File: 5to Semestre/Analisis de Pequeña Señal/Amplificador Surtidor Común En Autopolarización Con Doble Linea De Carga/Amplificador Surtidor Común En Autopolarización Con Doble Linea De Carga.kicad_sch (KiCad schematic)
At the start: 9 parts, among them Q1 NJFET

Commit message: añadiendo Rc para simulaciones con carga y uso de etiquetas
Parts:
- added Rc1: 100k, symbol Device:R
- Rd1: renamed from R2; value 6k -> 1k
- Rs1: renamed from R3; value 300 -> 1k
- renumbered R1 to Rg1
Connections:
- net 0: now also Rc1.2
- net Vdd: now reaches Rd1.1, V2.1
- net Vo: now reaches C3.2
- net Vo: now also Rc1.1
- net Vi: now reaches C1.1, V1.1
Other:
- moved on the sheet: V1, V2

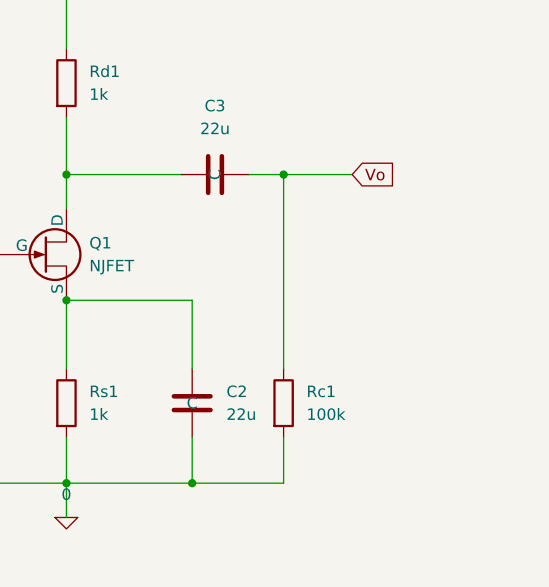
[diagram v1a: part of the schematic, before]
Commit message: obteniendo respuesta en frecuencia AC tipo boa comiendo un elefante con capacitancias parasitas
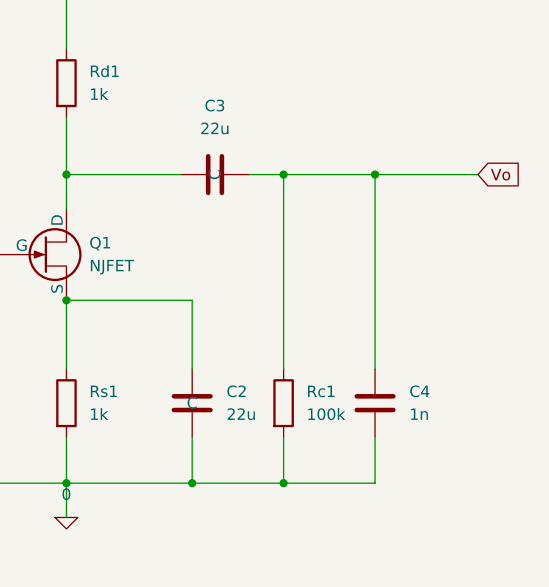
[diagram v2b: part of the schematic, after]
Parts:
- added C4: 1n, symbol Device:C
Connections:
- net 0: now also C4.2
- net Vo: now also C4.1
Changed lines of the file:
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@@
+	)
+	(junction
+		(at 165.1 123.19)
+		(diameter 0)
+		(color 0 0 0 0)
 	)
 	(junction
@@
 		(color 0 0 0 0)
 	)
+	(junction
+		(at 175.26 88.9)
+		(diameter 0)
+		(color 0 0 0 0)
+	)
+	(wire
+		(pts
+			(xy 175.26 118.11) (xy 175.26 123.19)
+		)
+		(stroke
+			(width 0)
+			(type default)
+		)
+	)
 	(wire
 		(pts
@@
 	(wire
 		(pts
+			(xy 175.26 88.9) (xy 186.69 88.9)
+		)
+		(stroke
+			(width 0)
+			(type default)
+		)
+	)
+	(wire
+		(pts
 			(xy 140.97 102.87) (xy 140.97 110.49)
 		)
@@
 	(wire
 		(pts
-			(xy 165.1 88.9) (xy 172.72 88.9)
+			(xy 165.1 88.9) (xy 175.26 88.9)
 		)
 		(stroke
@@
 	(wire
 		(pts
+			(xy 175.26 123.19) (xy 165.1 123.19)
+		)
+		(stroke
+			(width 0)
+			(type default)
+		)
+	)
+	(wire
+		(pts
 			(xy 127 123.19) (xy 140.97 123.19)
+		)
+		(stroke
+			(width 0)
+			(type default)
+		)
+	)
+	(wire
+		(pts
+			(xy 175.26 88.9) (xy 175.26 110.49)
 		)
 		(stroke
@@
 	(global_label "Vo"
 		(shape input)
-		(at 172.72 88.9 0)
+		(at 186.69 88.9 0)
 		(fields_autoplaced yes)
 		(effects
@@
 		)
 		(property "Intersheetrefs" "${INTERSHEET_REFS}"
-			(at 177.9428 88.9 0)
+			(at 191.9128 88.9 0)
 			(effects
 				(font
@@
 					(unit 1)
 				)
+			)
+		)
+	)
+	(symbol
+		(lib_id "Device:C")
+		(at 175.26 114.3 0)
+		(unit 1)
+		(exclude_from_sim no)
+		(in_bom yes)
+		(on_board yes)
+		(dnp no)
+		(fields_autoplaced yes)
+		(property "Reference" "C4"
+			(at 179.07 113.0299 0)
+			(effects
+				(font
+					(size 1.27 1.27)
+				)
+				(justify left)
+			)
+		)
+		(property "Value" "1n"
+			(at 179.07 115.5699 0)
+			(effects
+				(font
+					(size 1.27 1.27)
+				)
+				(justify left)
+			)
+		)
+		(property "Footprint" ""
+			(at 176.2252 118.11 0)
+			(effects
+				(font
+					(size 1.27 1.27)
+				)
+				(hide yes)
+			)
+		)
+		(property "Datasheet" "~"
+			(at 175.26 114.3 0)
+			(effects
+				(font
+					(size 1.27 1.27)
+				)
+				(hide yes)
+			)
+		)
+		(property "Description" "Unpolarized capacitor"
+			(at 175.26 114.3 0)
+			(effects
+				(font
+					(size 1.27 1.27)
+				)
+				(hide yes)
+			)
+		)
+		(pin "1"
+		)
+		(pin "2"
+		)
+		(instances
+			(project "Amplificador Surtidor Común En Autopolarización Con Doble Linea De Carga"
+				(path "/cec29d34-94dc-4fef-8b65-c8bf40701861"
+					(reference "C4")
+					(unit 1)
+				)
